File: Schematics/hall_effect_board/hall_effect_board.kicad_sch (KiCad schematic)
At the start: 5 parts, among them J1 B04B-PASK, U1 TMAG5273A1QDBVT

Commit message: cleaned up hall effect, switched to plated through holes
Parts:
- H1, H2: footprint MountingHole:MountingHole_3.2mm_M3 -> MountingHole:MountingHole_3.2mm_M3_ISO14580_Pad
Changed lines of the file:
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@@
 			)
 		)
-		(property "Footprint" "MountingHole:MountingHole_3.2mm_M3"
+		(property "Footprint" "MountingHole:MountingHole_3.2mm_M3_ISO14580_Pad"
 			(at 156.21 86.36 0)
 			(effects
@@
 			)
 		)
-		(property "Footprint" "MountingHole:MountingHole_3.2mm_M3"
+		(property "Footprint" "MountingHole:MountingHole_3.2mm_M3_ISO14580_Pad"
 			(at 156.21 80.01 0)
 			(effects

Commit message: update for emily!!
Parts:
- removed J1: B04B-PASK, footprints:CONN_B04B-PASK_JST, symbol Connector:Conn_01x04_Pin
- added J3: HALL-1, footprints:CONN_SD-105309-100_04_MOL, symbol Connector_Generic:Conn_01x04
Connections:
- net +3V3: now also J3.1 (Pin_1)
- net GND: now also J3.4 (Pin_4)
- net SCA: now also J3.2 (Pin_2)
- net SCL: now also J3.3 (Pin_3)

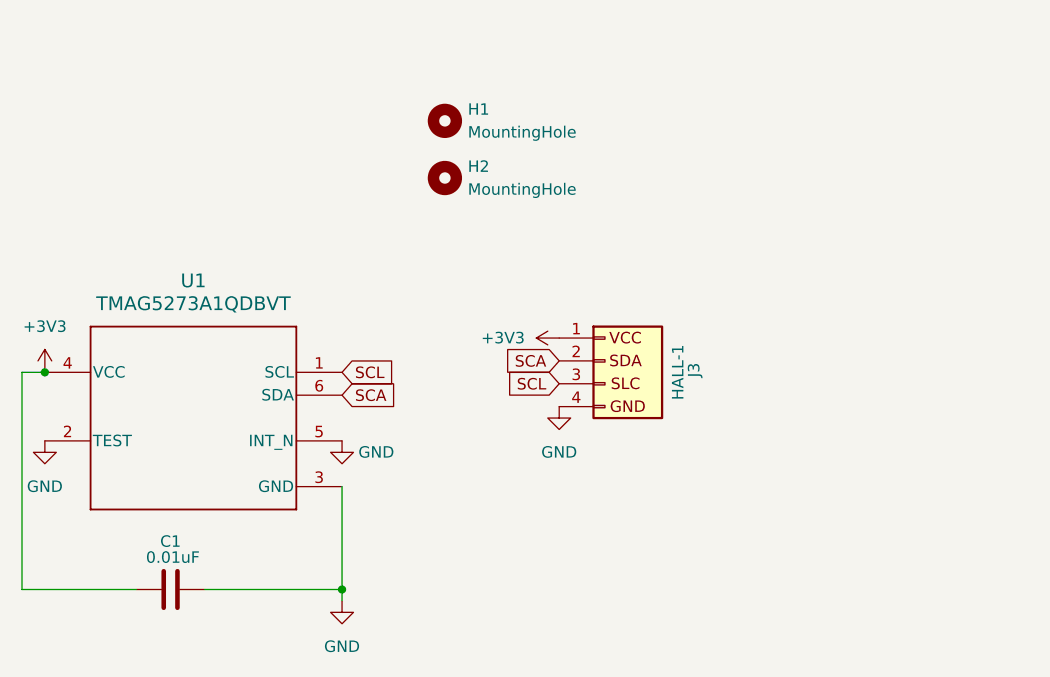
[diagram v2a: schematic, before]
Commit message: update schematic pin names
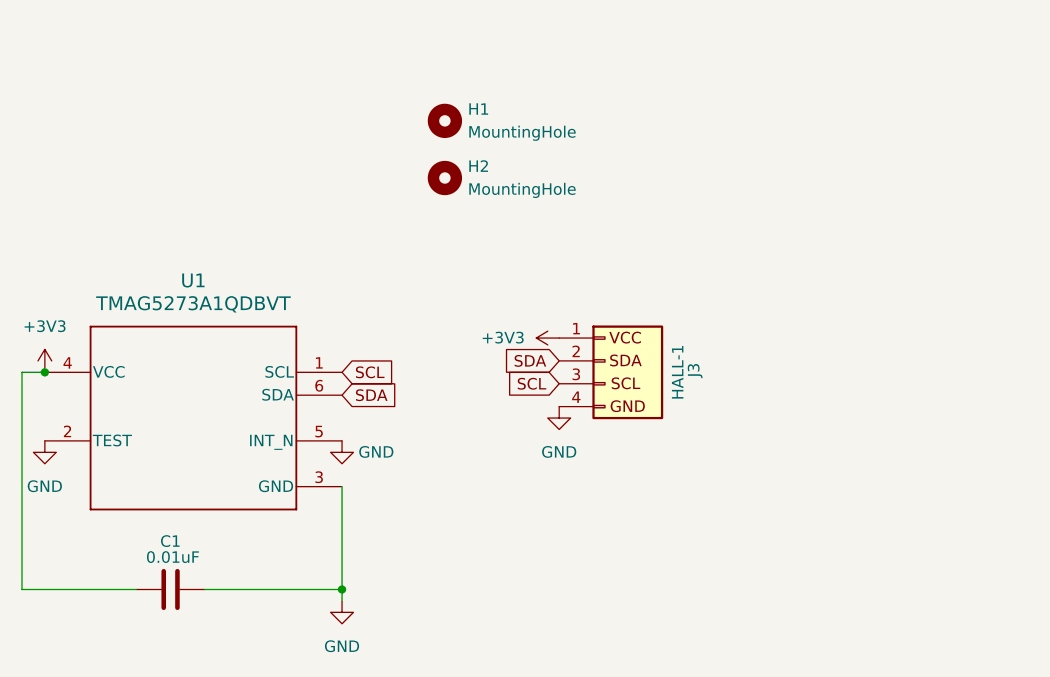
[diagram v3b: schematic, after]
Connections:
- net SCA renamed SDA
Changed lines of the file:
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@@
 		)
 	)
-	(global_label "SCA"
+	(global_label "SDA"
 		(shape input)
 		(at 168.91 106.68 180)
@@
 		)
 	)
-	(global_label "SCA"
+	(global_label "SDA"
 		(shape input)
 		(at 144.78 110.49 0)

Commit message: Footprint Update
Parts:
- J3: footprint footprints:CONN_SD-105309-100_04_MOL -> Connector_Molex:Molex_Nano-Fit_105313-xx04_1x04_P2.50mm_Horizontal
- U1: footprint DBV0006A-IPC_A -> footprints:DBV0006A-IPC_A
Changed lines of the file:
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@@
 			)
 		)
-		(property "Footprint" "footprints:CONN_SD-105309-100_04_MOL"
+		(property "Footprint" "Connector_Molex:Molex_Nano-Fit_105313-xx04_1x04_P2.50mm_Horizontal"
 			(at 173.99 106.68 0)
 			(effects
@@
 			)
 		)
-		(property "Footprint" "DBV0006A-IPC_A"
+		(property "Footprint" "footprints:DBV0006A-IPC_A"
 			(at 111.76 107.95 0)
 			(effects

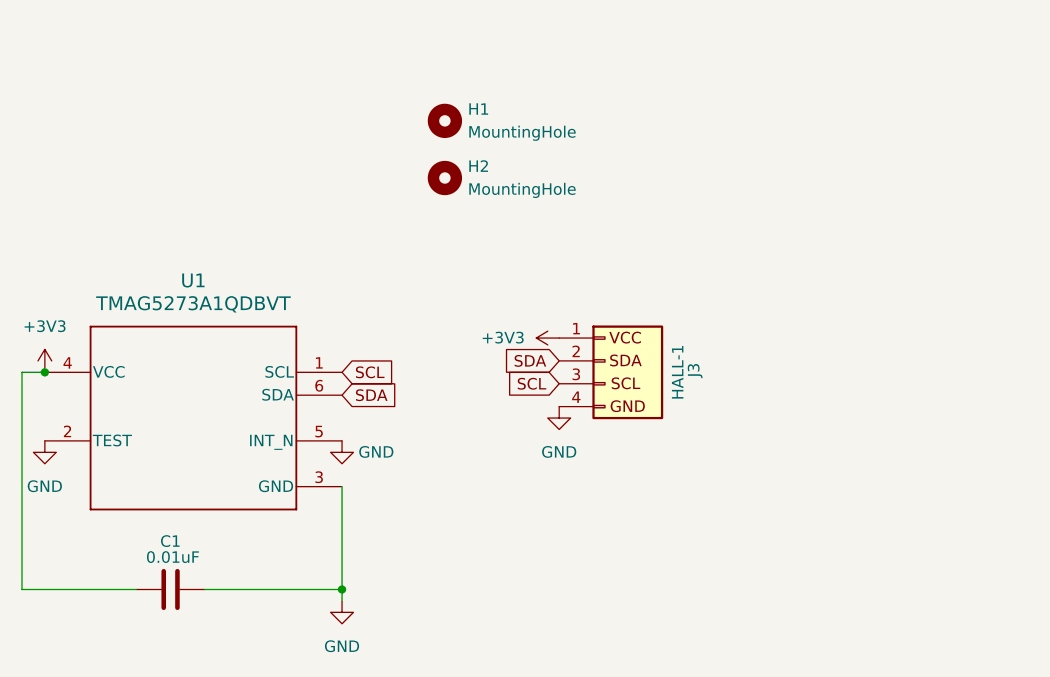
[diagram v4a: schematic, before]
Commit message: Found issue on hall board, only effects LED
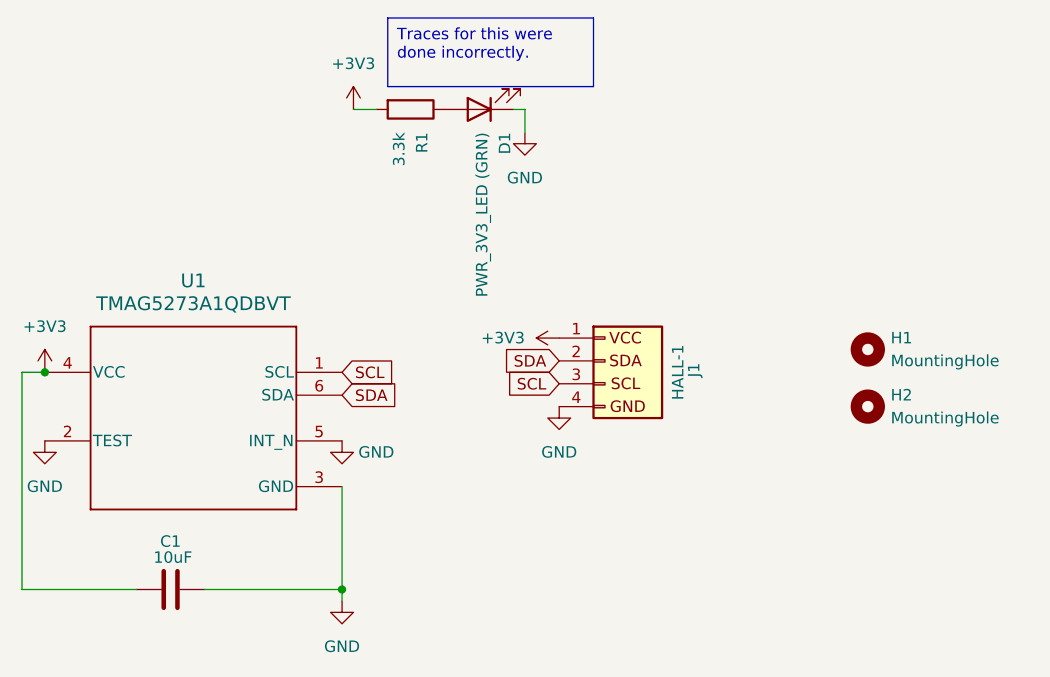
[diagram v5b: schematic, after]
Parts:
- added D1: PWR_3V3_LED (GRN), LED_SMD:LED_0603_1608Metric, symbol Device:LED
- added R1: 3.3k, Resistor_SMD:R_0603_1608Metric, symbol Device:R
- C1: value 0.01uF -> 10uF; Digikey 399-C0805X103K5RAC7210CT-ND -> (none); JLCSC (none) -> C15850
- renumbered J3 to J1
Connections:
- net +3V3: now also R1.2
- net GND: now also D1.1 (K)
- new net: D1.2 (A), R1.1
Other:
- moved on the sheet: H1, H2
